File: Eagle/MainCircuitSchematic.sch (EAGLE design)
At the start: 13 parts

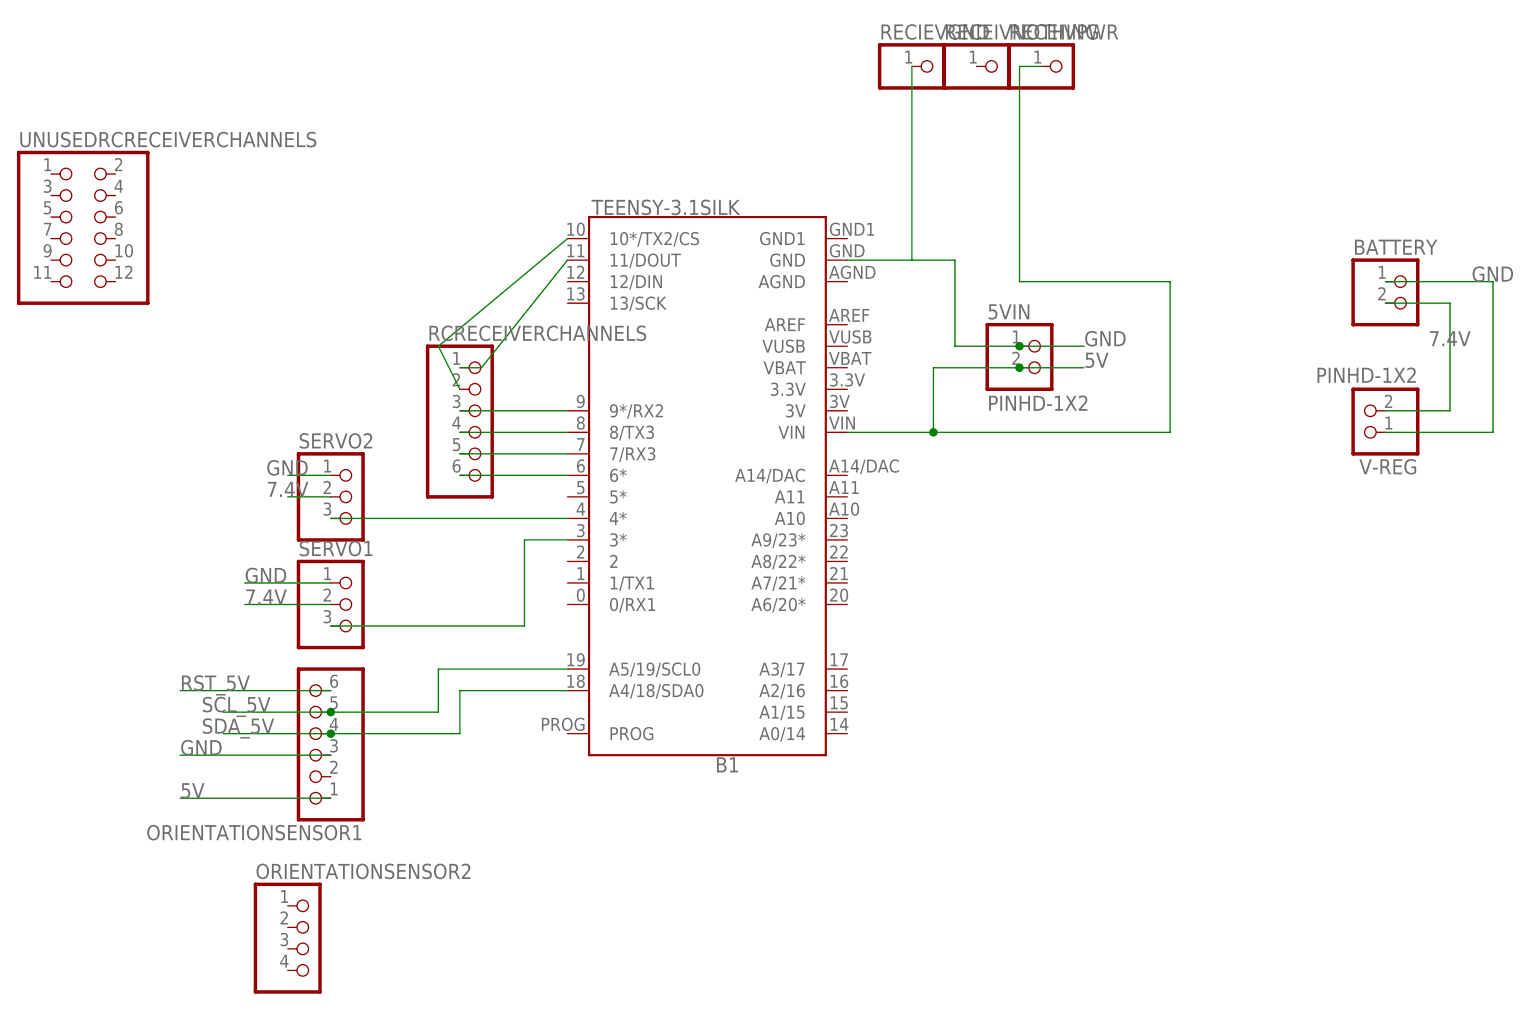
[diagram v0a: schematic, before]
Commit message: added switch to design, removed excess receiver pins
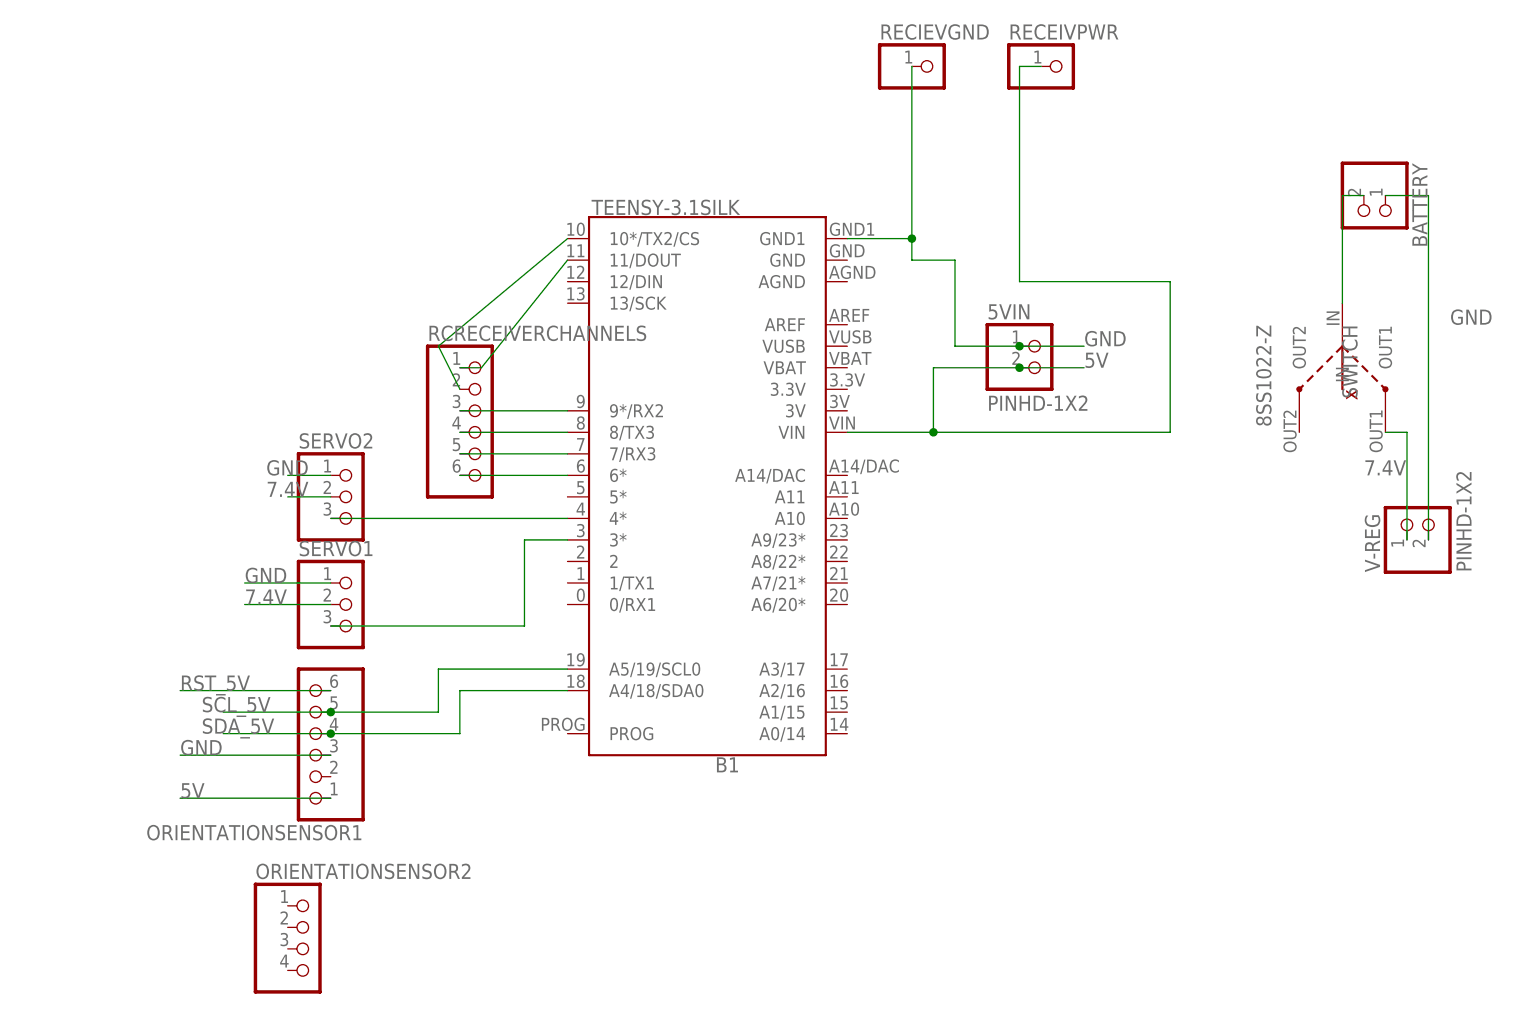
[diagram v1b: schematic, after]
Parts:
- removed RECEIVNOTHING: (no value), pinhead:PINHD-1X1
- removed UNUSEDRCRECEIVERCHANNELS: PINHD-2X6, Connector:PINHD-2X6
- added SWITCH: 8SS1022-Z, ornithopter:8SS1022-Z
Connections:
- new net N$9: BATTERY.2, SWITCH.IN
- net 7.4V: now also SWITCH.OUT1, V-REG.1; no longer BATTERY.2, V-REG.2
- net GND: now also B1.GND1, V-REG.2; no longer B1.GND, V-REG.1
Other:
- moved on the sheet: BATTERY, V-REG
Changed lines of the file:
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@@
 <part name="V-REG" library="Connector" library_urn="urn:adsk.eagle:library:16378166" deviceset="PINHD-1X2" device="" package3d_urn="urn:adsk.eagle:package:22435/2"/>
 <part name="5VIN" library="Connector" library_urn="urn:adsk.eagle:library:16378166" deviceset="PINHD-1X2" device="" package3d_urn="urn:adsk.eagle:package:22435/2"/>
-<part name="UNUSEDRCRECEIVERCHANNELS" library="Connector" library_urn="urn:adsk.eagle:library:16378166" deviceset="PINHD-2X6" device="" package3d_urn="urn:adsk.eagle:package:22474/2"/>
 <part name="RECIEVGND" library="pinhead" library_urn="urn:adsk.eagle:library:325" deviceset="PINHD-1X1" device="" package3d_urn="urn:adsk.eagle:package:22485/2"/>
-<part name="RECEIVNOTHING" library="pinhead" library_urn="urn:adsk.eagle:library:325" deviceset="PINHD-1X1" device="" package3d_urn="urn:adsk.eagle:package:22485/2"/>
 <part name="RECEIVPWR" library="pinhead" library_urn="urn:adsk.eagle:library:325" deviceset="PINHD-1X1" device="" package3d_urn="urn:adsk.eagle:package:22485/2"/>
+<part name="SWITCH" library="ornithopter" deviceset="8SS1022-Z" device=""/>
 </parts>
 <sheets>
@@
 <attribute name="VALUE" x="46.99" y="58.42" size="1.778" layer="96"/>
 </instance>
-<instance part="BATTERY" gate="G$1" x="162.56" y="83.82" smashed="yes">
-<attribute name="NAME" x="156.21" y="89.535" size="1.778" layer="95"/>
-</instance>
-<instance part="V-REG" gate="G$1" x="157.48" y="71.12" smashed="yes" rot="R180">
-<attribute name="NAME" x="163.83" y="65.405" size="1.778" layer="95" rot="R180"/>
-<attribute name="VALUE" x="163.83" y="76.2" size="1.778" layer="96" rot="R180"/>
+<instance part="BATTERY" gate="G$1" x="157.48" y="93.98" smashed="yes" rot="R270">
+<attribute name="NAME" x="163.195" y="100.33" size="1.778" layer="95" rot="R270"/>
+</instance>
+<instance part="V-REG" gate="G$1" x="165.1" y="58.42" smashed="yes" rot="R90">
+<attribute name="NAME" x="159.385" y="52.07" size="1.778" layer="95" rot="R90"/>
+<attribute name="VALUE" x="170.18" y="52.07" size="1.778" layer="96" rot="R90"/>
 </instance>
 <instance part="5VIN" gate="G$1" x="119.38" y="76.2" smashed="yes">
@@
 <attribute name="VALUE" x="113.03" y="71.12" size="1.778" layer="96"/>
 </instance>
-<instance part="UNUSEDRCRECEIVERCHANNELS" gate="A" x="5.08" y="93.98" smashed="yes">
-<attribute name="NAME" x="-1.27" y="102.235" size="1.778" layer="95"/>
-</instance>
 <instance part="RECIEVGND" gate="G$1" x="106.68" y="111.76" smashed="yes">
 <attribute name="NAME" x="100.33" y="114.935" size="1.778" layer="95"/>
 <attribute name="VALUE" x="100.33" y="106.68" size="1.778" layer="96"/>
 </instance>
-<instance part="RECEIVNOTHING" gate="G$1" x="114.3" y="111.76" smashed="yes">
-<attribute name="NAME" x="107.95" y="114.935" size="1.778" layer="95"/>
-<attribute name="VALUE" x="107.95" y="106.68" size="1.778" layer="96"/>
-</instance>
 <instance part="RECEIVPWR" gate="G$1" x="121.92" y="111.76" smashed="yes">
 <attribute name="NAME" x="115.57" y="114.935" size="1.778" layer="95"/>
 <attribute name="VALUE" x="115.57" y="106.68" size="1.778" layer="96"/>
+</instance>
+<instance part="SWITCH" gate="G$1" x="154.94" y="78.74" smashed="yes" rot="R270">
+<attribute name="NAME" x="154.94" y="81.28" size="1.778" layer="95" rot="R270"/>
+<attribute name="VALUE" x="144.78" y="81.28" size="1.778" layer="96" rot="R270"/>
 </instance>
 </instances>
@@
 <wire x1="35.56" y1="50.8" x2="25.4" y2="50.8" width="0.1524" layer="91"/>
 <label x="25.4" y="50.8" size="1.778" layer="95"/>
-</segment>
-<segment>
-<pinref part="BATTERY" gate="G$1" pin="1"/>
-<wire x1="172.72" y1="86.36" x2="160.02" y2="86.36" width="0.1524" layer="91"/>
-<label x="170.18" y="86.36" size="1.778" layer="95"/>
-<pinref part="V-REG" gate="G$1" pin="1"/>
-<wire x1="172.72" y1="86.36" x2="172.72" y2="68.58" width="0.1524" layer="91"/>
-<wire x1="172.72" y1="68.58" x2="160.02" y2="68.58" width="0.1524" layer="91"/>
 </segment>
 <segment>
@@
 <wire x1="109.22" y1="78.74" x2="109.22" y2="88.9" width="0.1524" layer="91"/>
 <junction x="116.84" y="78.74"/>
-<pinref part="B1" gate="G$1" pin="GND"/>
-<wire x1="104.14" y1="88.9" x2="96.52" y2="88.9" width="0.1524" layer="91"/>
 <pinref part="RECIEVGND" gate="G$1" pin="1"/>
 <wire x1="109.22" y1="88.9" x2="104.14" y2="88.9" width="0.1524" layer="91"/>
-<wire x1="104.14" y1="88.9" x2="104.14" y2="111.76" width="0.1524" layer="91"/>
+<wire x1="104.14" y1="88.9" x2="104.14" y2="91.44" width="0.1524" layer="91"/>
+<pinref part="B1" gate="G$1" pin="GND1"/>
+<wire x1="104.14" y1="91.44" x2="104.14" y2="111.76" width="0.1524" layer="91"/>
+<wire x1="96.52" y1="91.44" x2="104.14" y2="91.44" width="0.1524" layer="91"/>
+<junction x="104.14" y="91.44"/>
 </segment>
 <segment>
@@
 <wire x1="35.56" y1="30.48" x2="17.78" y2="30.48" width="0.1524" layer="91"/>
 <label x="17.78" y="30.48" size="1.778" layer="95"/>
+</segment>
+<segment>
+<pinref part="BATTERY" gate="G$1" pin="1"/>
+<pinref part="V-REG" gate="G$1" pin="2"/>
+<wire x1="160.02" y1="96.52" x2="165.1" y2="96.52" width="0.1524" layer="91"/>
+<wire x1="165.1" y1="96.52" x2="165.1" y2="55.88" width="0.1524" layer="91"/>
+<label x="167.64" y="81.28" size="1.778" layer="95"/>
 </segment>
 </net>
@@
 <net name="7.4V" class="0">
 <segment>
-<pinref part="BATTERY" gate="G$1" pin="2"/>
-<wire x1="167.64" y1="83.82" x2="160.02" y2="83.82" width="0.1524" layer="91"/>
-<label x="165.1" y="78.74" size="1.778" layer="95"/>
-<pinref part="V-REG" gate="G$1" pin="2"/>
-<wire x1="167.64" y1="83.82" x2="167.64" y2="71.12" width="0.1524" layer="91"/>
-<wire x1="167.64" y1="71.12" x2="160.02" y2="71.12" width="0.1524" layer="91"/>
-</segment>
-<segment>
 <pinref part="SERVO2" gate="A" pin="2"/>
 <wire x1="35.56" y1="60.96" x2="30.48" y2="60.96" width="0.1524" layer="91"/>
@@
 <wire x1="35.56" y1="48.26" x2="25.4" y2="48.26" width="0.1524" layer="91"/>
 <label x="25.4" y="48.26" size="1.778" layer="95"/>
+</segment>
+<segment>
+<pinref part="SWITCH" gate="G$1" pin="OUT1"/>
+<pinref part="V-REG" gate="G$1" pin="1"/>
+<wire x1="160.02" y1="68.58" x2="162.56" y2="68.58" width="0.1524" layer="91"/>
+<wire x1="162.56" y1="68.58" x2="162.56" y2="55.88" width="0.1524" layer="91"/>
+<label x="157.48" y="63.5" size="1.778" layer="95"/>
 </segment>
 </net>
@@
 </segment>
 </net>
+<net name="N$9" class="0">
+<segment>
+<pinref part="BATTERY" gate="G$1" pin="2"/>
+<pinref part="SWITCH" gate="G$1" pin="IN"/>
+<wire x1="157.48" y1="96.52" x2="154.94" y2="96.52" width="0.1524" layer="91"/>
+<wire x1="154.94" y1="96.52" x2="154.94" y2="83.82" width="0.1524" layer="91"/>
+</segment>
+</net>
